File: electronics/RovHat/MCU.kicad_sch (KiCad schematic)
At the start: 26 parts, among them J301 PICO_1-20, J302 PICO_SWD, J303 Conn_01x02, J304 PICO_21-40, J305 SWD_EXT, U301 W25Q128JVS, U302 ASDMB-xxxMHz, U303 RP2040

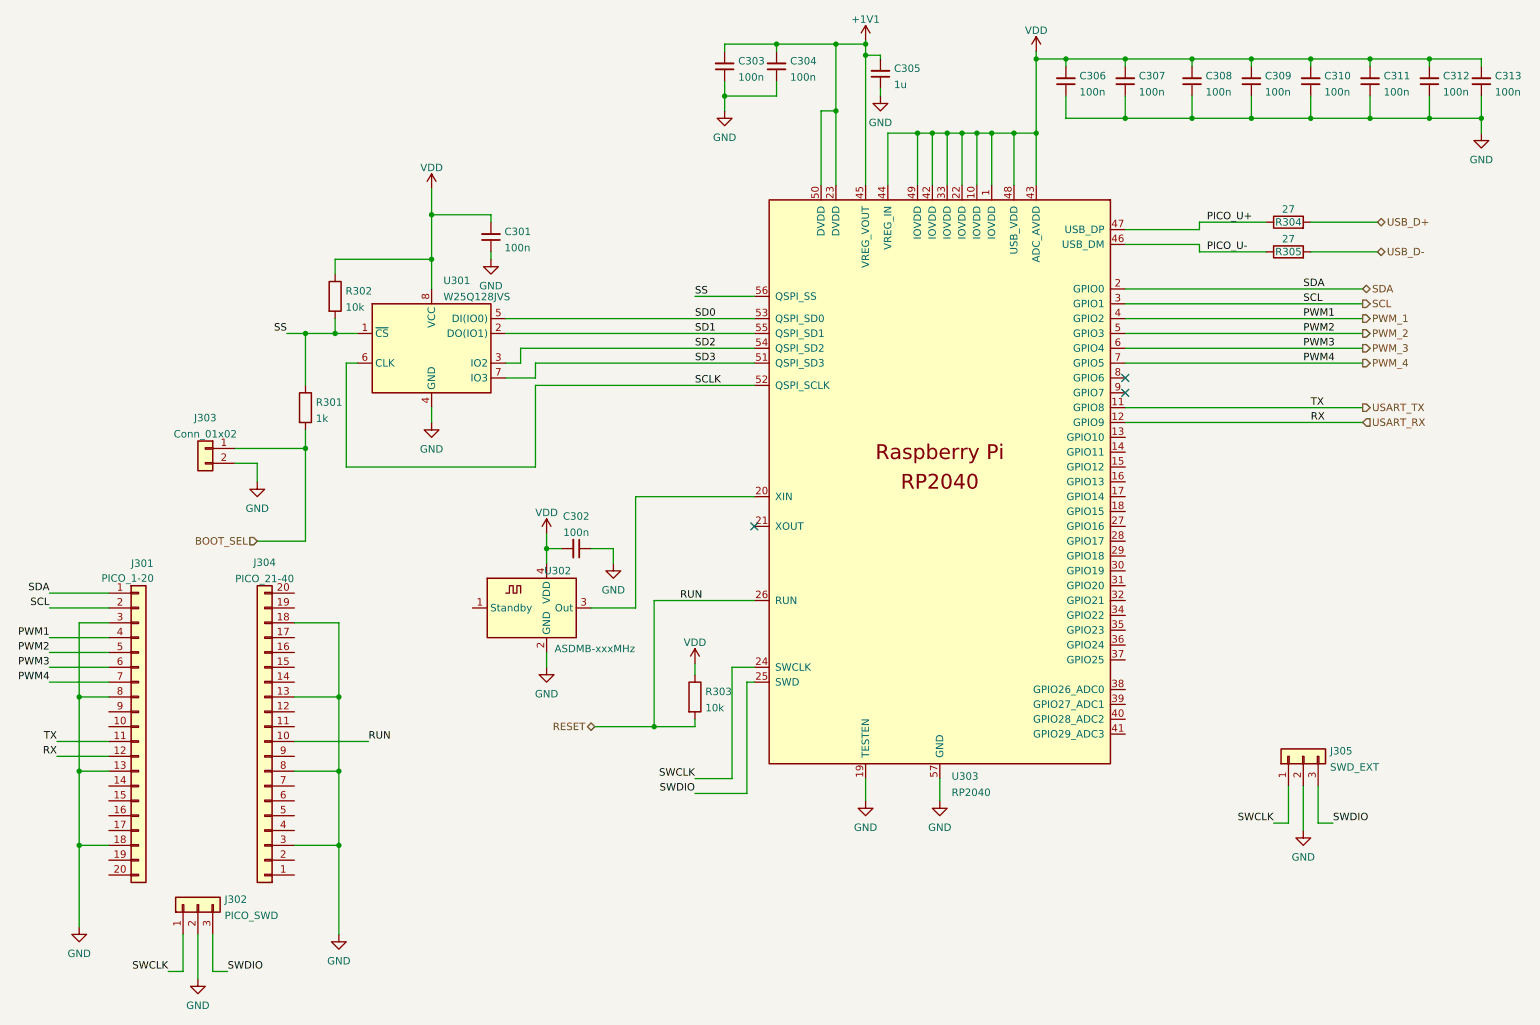
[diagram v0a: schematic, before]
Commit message: Changed To RPI Pico Module
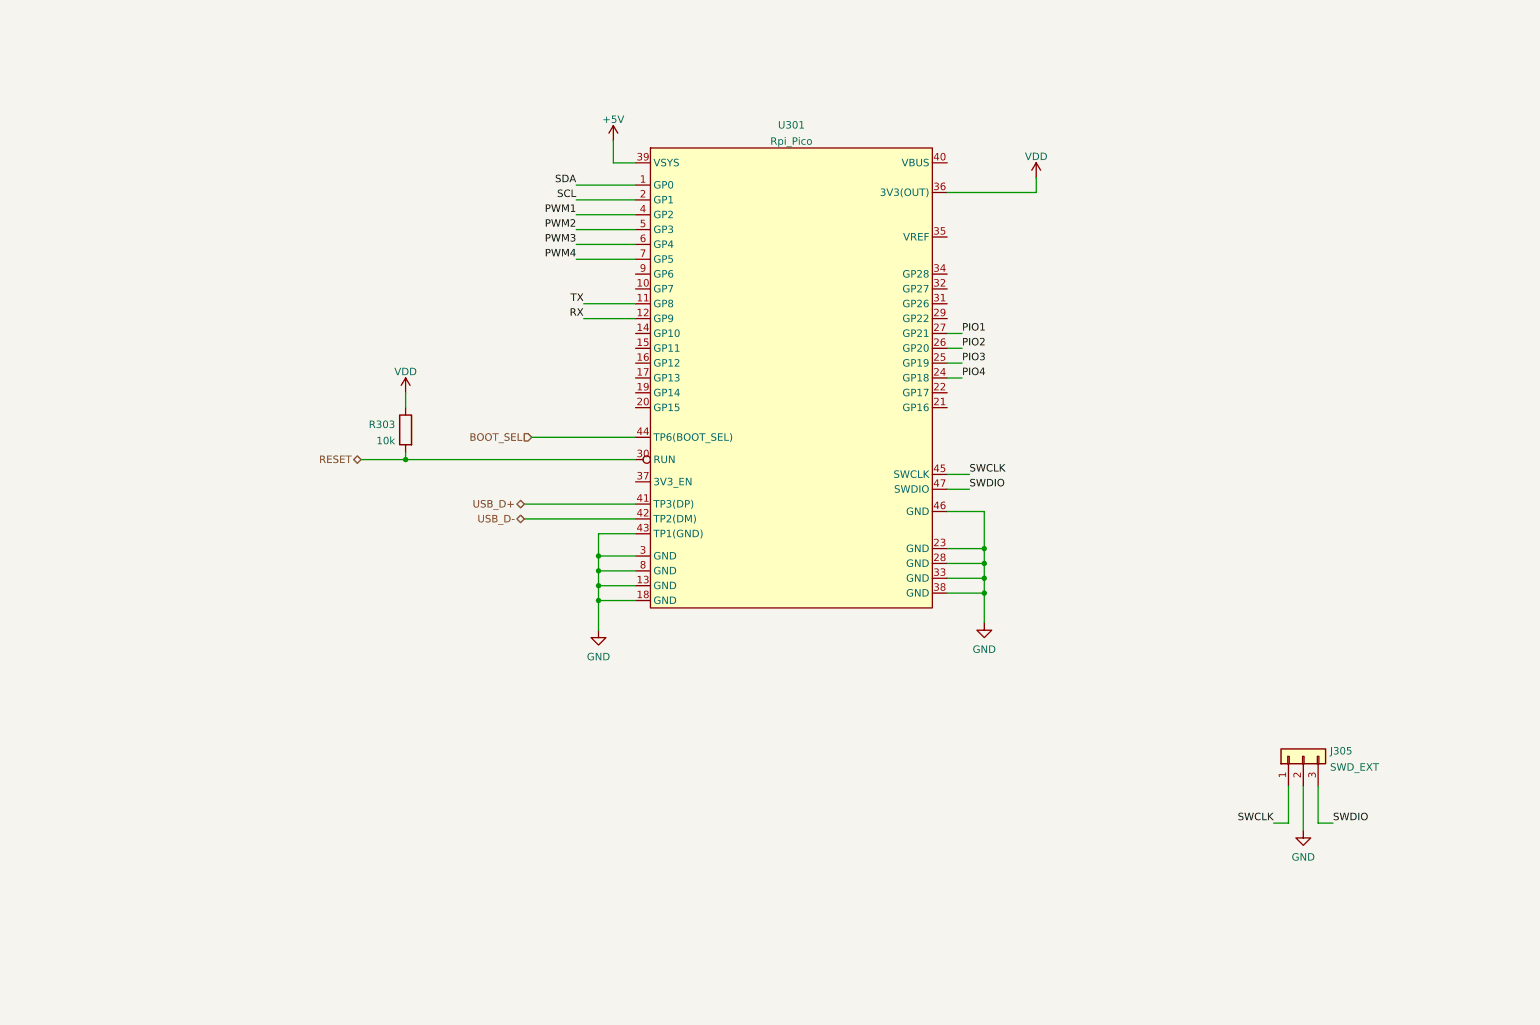
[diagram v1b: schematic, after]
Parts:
- removed C301, C302, C303, C304, C306, C307, C308, C309, C310, C311, C312, C313: 100n, Capacitor_SMD:C_0201_0603Metric, symbol Device:C_Small
- removed C305: 1u, Capacitor_SMD:C_0805_2012Metric, symbol Device:C_Small
- removed J301: PICO_1-20, Connector_PinHeader_2.54mm:PinHeader_1x20_P2.54mm_Vertical, symbol Connector_Generic:Conn_01x20
- removed J302: PICO_SWD, Connector_PinHeader_2.54mm:PinHeader_1x03_P2.54mm_Vertical, symbol Connector_Generic:Conn_01x03
- removed J303: Conn_01x02, Connector_PinHeader_2.54mm:PinHeader_1x02_P2.54mm_Vertical, symbol Connector_Generic:Conn_01x02
- removed J304: PICO_21-40, Connector_PinHeader_2.54mm:PinHeader_1x20_P2.54mm_Vertical, symbol Connector_Generic:Conn_01x20
- removed R301: 1k, Resistor_SMD:R_0603_1608Metric, symbol Device:R
- removed R302: 10k, Resistor_SMD:R_0603_1608Metric, symbol Device:R
- removed R304, R305: 27, Resistor_SMD:R_0402_1005Metric, symbol Device:R
- removed U301: W25Q128JVS, Package_SO:SOIC-8_5.23x5.23mm_P1.27mm, symbol Memory_Flash:W25Q128JVS
- removed U302: ASDMB-xxxMHz, Oscillator:Oscillator_SMD_Abracon_ASDMB-4Pin_2.5x2.0mm, symbol Oscillator:ASDMB-xxxMHz
- removed U303: RP2040, Findersee_parts:RP2040-QFN-56, symbol Findersee_parts:RP2040
- added U301: Rpi_Pico, Findersee_parts:RP_PICO, symbol Findersee_parts:Rpi_Pico
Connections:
- net BOOT_SEL: now also U301.44 (TP6(BOOT_SEL))
- net GND: now also U301.13 (GND), U301.18 (GND), U301.23 (GND), U301.28 (GND), U301.3 (GND), U301.33 (GND), U301.38 (GND), U301.43 (TP1(GND)), U301.46 (GND), U301.8 (GND)
- net RESET: now also U301.30 (RUN)
- net SCL: now also U301.2 (GP1)
- net SDA: now also U301.1 (GP0)
- net SWCLK: now also U301.45 (SWCLK)
- net SWDIO: now also U301.47 (SWDIO)
- net USB_D+: now also U301.41 (TP3(DP))
- net USB_D-: now also U301.42 (TP2(DM))
- net VDD: now also U301.36 (3V3(OUT))
- new net +5V: U301.39 (VSYS)
- new net PIO1: U301.27 (GP21)
- new net PIO2: U301.26 (GP20)
- new net PIO3: U301.25 (GP19)
- new net PIO4: U301.24 (GP18)
- new net PWM1: U301.4 (GP2)
- new net PWM2: U301.5 (GP3)
- new net PWM3: U301.6 (GP4)
- new net PWM4: U301.7 (GP5)
- new net RX: U301.12 (GP9)
- new net TX: U301.11 (GP8)
- no-connect marks 3 -> 0
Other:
- moved on the sheet: R303

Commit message: Layout Done first level
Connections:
- net PIO1: now also U301.34 (GP28); no longer U301.27 (GP21)
- net PIO2: now also U301.32 (GP27); no longer U301.26 (GP20)
- net PIO3: now also U301.31 (GP26); no longer U301.25 (GP19)
- net PIO4: now also U301.29 (GP22); no longer U301.24 (GP18)
- net LSM_DRDY: now reaches U301.14 (GP10)
- net LSM_INT2: now reaches U301.15 (GP11)
- net LSM_INT1: now reaches U301.16 (GP12)
- net GYRO_RDY: now reaches U301.17 (GP13)
- net GYRO_INT: now reaches U301.19 (GP14)
- net PWM_4: now reaches U301.21 (GP16)
- net PWM_3: now reaches U301.22 (GP17)
- net VBUS: now reaches U301.40 (VBUS)
- net PWM1: no longer names the net of U301.4 (GP2)
- net PWM2: no longer names the net of U301.5 (GP3)
- net PWM3: no longer names the net of U301.6 (GP4)
- net PWM4: no longer names the net of U301.7 (GP5)
- net RX renamed USART_RX
- net TX renamed USART_TX
- new net PWM_1: U301.25 (GP19)
- new net PWM_2: U301.24 (GP18)
- no-connect marks 0 -> 11
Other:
- moved on the sheet: R303, U301

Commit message: Fabrication commit
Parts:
- added J301: PWM_OUT, Connector_PinHeader_2.54mm:PinHeader_1x03_P2.54mm_Vertical, symbol Connector_Generic:Conn_01x03
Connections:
- net GND: now also J301.1 (Pin_1)
- net at U301.10 (GP7): now also J301.3 (Pin_3)
- net ADS_RDY: now reaches U301.27 (GP21)
- net at U301.9 (GP6): now also J301.2 (Pin_2)
- no-connect marks 11 -> 8
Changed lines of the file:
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@@
   (junction (at 201.93 102.87) (diameter 0) (color 0 0 0 0)
   )
-  (no_connect (at 195.58 41.91))
   (no_connect (at 142.24 71.12))
+  (no_connect (at 195.58 60.96))
+  (no_connect (at 195.58 41.91))
   (no_connect (at 142.24 83.82))
-  (no_connect (at 142.24 50.8))
-  (no_connect (at 142.24 48.26))
   (no_connect (at 142.24 43.18))
   (no_connect (at 142.24 45.72))
   (no_connect (at 142.24 40.64))
   (no_connect (at 142.24 38.1))
-  (no_connect (at 195.58 58.42))
-  (no_connect (at 195.58 60.96))
   (wire (pts (xy 102.87 68.58) (xy 102.87 71.12))
     (stroke (width 0) (type default) (color 0 0 0 0))
@@
     (stroke (width 0) (type default) (color 0 0 0 0))
   )
+  (wire (pts (xy 115.57 48.26) (xy 142.24 48.26))
+    (stroke (width 0) (type default) (color 0 0 0 0))
+  )
   (wire (pts (xy 205.74 66.04) (xy 195.58 66.04))
     (stroke (width 0) (type default) (color 0 0 0 0))
@@
     (stroke (width 0) (type default) (color 0 0 0 0))
   )
+  (wire (pts (xy 115.57 45.72) (xy 118.11 45.72))
+    (stroke (width 0) (type default) (color 0 0 0 0))
+  )
   (wire (pts (xy 123.19 90.17) (xy 142.24 90.17))
     (stroke (width 0) (type default) (color 0 0 0 0))
@@
     (stroke (width 0) (type default) (color 0 0 0 0))
   )
+  (wire (pts (xy 115.57 50.8) (xy 142.24 50.8))
+    (stroke (width 0) (type default) (color 0 0 0 0))
+  )
   (wire (pts (xy 102.87 78.74) (xy 102.87 80.01))
     (stroke (width 0) (type default) (color 0 0 0 0))
@@
     (stroke (width 0) (type default) (color 0 0 0 0))
   )
+  (wire (pts (xy 195.58 58.42) (xy 205.74 58.42))
+    (stroke (width 0) (type default) (color 0 0 0 0))
+  )
+  (wire (pts (xy 118.11 45.72) (xy 118.11 55.88))
+    (stroke (width 0) (type default) (color 0 0 0 0))
+  )
   (wire (pts (xy 205.74 63.5) (xy 195.58 63.5))
     (stroke (width 0) (type default) (color 0 0 0 0))
@@
     (effects (font (size 1.27 1.27)) (justify right))
   )
+  (hierarchical_label "ADS_RDY" (shape input) (at 205.74 58.42 0)
+    (effects (font (size 1.27 1.27)) (justify left))
+  )
   (hierarchical_label "PWM_1" (shape output) (at 205.74 63.5 0)
     (effects (font (size 1.27 1.27)) (justify left))
@@
     (pin "2")
   )
+  (symbol (lib_id "power:GND") (at 118.11 55.88 0) (unit 1)
+    (in_bom yes) (on_board yes) (fields_autoplaced)
+    (property "Reference" "#PWR0301" (id 0) (at 118.11 62.23 0)
+      (effects (font (size 1.27 1.27)) hide)
+    )
+    (property "Value" "GND" (id 1) (at 118.11 60.4425 0))
+    (property "Footprint" "" (id 2) (at 118.11 55.88 0)
+      (effects (font (size 1.27 1.27)) hide)
+    )
+    (property "Datasheet" "" (id 3) (at 118.11 55.88 0)
+      (effects (font (size 1.27 1.27)) hide)
+    )
+    (pin "1")
+  )
   (symbol (lib_id "power:GND") (at 135.89 109.22 0) (unit 1)
     (in_bom yes) (on_board yes) (fields_autoplaced)
@@
     (pin "1")
   )
+  (symbol (lib_id "Connector_Generic:Conn_01x03") (at 110.49 48.26 0) (mirror y) (unit 1)
+    (in_bom yes) (on_board yes) (fields_autoplaced)
+    (property "Reference" "J301" (id 0) (at 110.49 40.4835 0))
+    (property "Value" "PWM_OUT" (id 1) (at 110.49 43.2586 0))
+    (property "Footprint" "Connector_PinHeader_2.54mm:PinHeader_1x03_P2.54mm_Vertical" (id 2) (at 110.49 48.26 0)
+      (effects (font (size 1.27 1.27)) hide)
+    )
+    (property "Datasheet" "~" (id 3) (at 110.49 48.26 0)
+      (effects (font (size 1.27 1.27)) hide)
+    )
+    (pin "1")
+    (pin "2")
+    (pin "3")
+  )
   (symbol (lib_id "power:GND") (at 201.93 107.95 0) (unit 1)

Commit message: Fabrication commit 2
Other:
- company: (none) -> Findersee
- title: (none) -> ROV RPI PICO HAT
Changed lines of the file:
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@@
 (kicad_sch (version 20211123) (generator eeschema)
   (paper "A4")
+  (title_block
+    (title "ROV RPI PICO HAT")
+    (date "2023-01-14")
+    (rev "1")
+    (company "Findersee")
+    (comment 1 "ROV RPI PICO HAT")
+  )
   (junction (at 135.89 99.06) (diameter 0) (color 0 0 0 0)
   )
